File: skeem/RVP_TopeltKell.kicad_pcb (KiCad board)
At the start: 2 copper layers, 106 x 91 mm, 84 parts, among them J1 Barrel_Jack, J10 Conn_01x03_Pin, J11 Conn_01x03_Pin, J12 Conn_01x03_Pin, J13 Conn_01x03_Pin, J14 Conn_01x03_Pin, J15 JST XH 5 pin, J16 JST XH 5 pin, J2 USB_B_Mini, J3 Conn_01x03_Pin, J4 Conn_01x03_Pin, J5 Conn_01x03_Pin, J6 Conn_01x03_Pin, J7 Conn_01x03_Pin, J8 Conn_01x03_Pin, J9 Conn_01x03_Pin, SW1 SW_RESET, U1 AP62200, U10 DRV8428, U11 DRV8428, U2 AP62200, U3 CP2102N-Axx-xQFN24, U4 ESP32-S3-WROOM-1-N4, U5 TLV4961, U6 TLV4961, U7 74LVC2G53, U8 74HCT4851, U9 74HCT4851

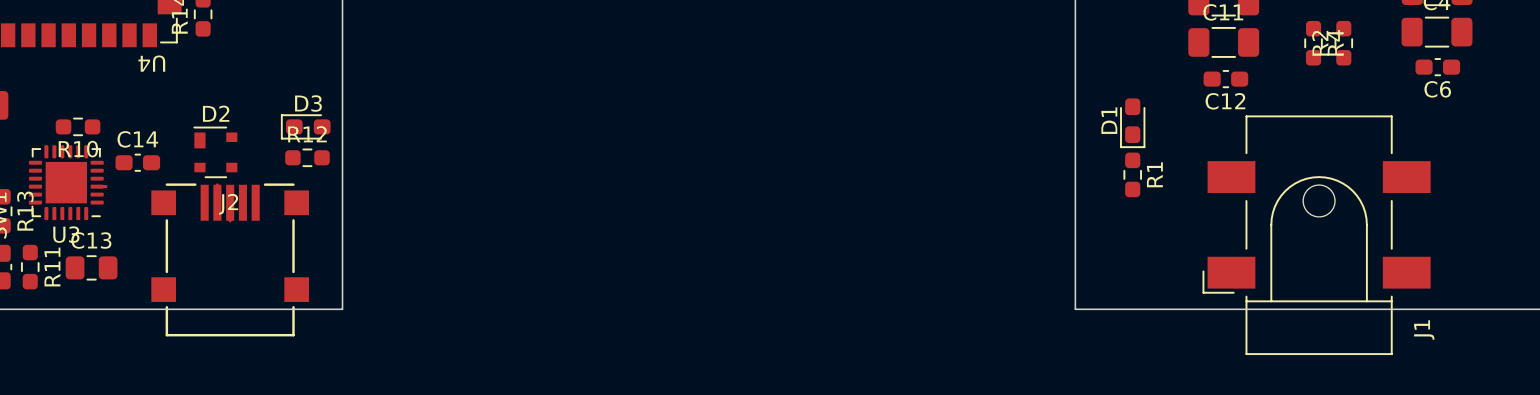
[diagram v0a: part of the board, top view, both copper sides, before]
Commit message: 3d models for pcb
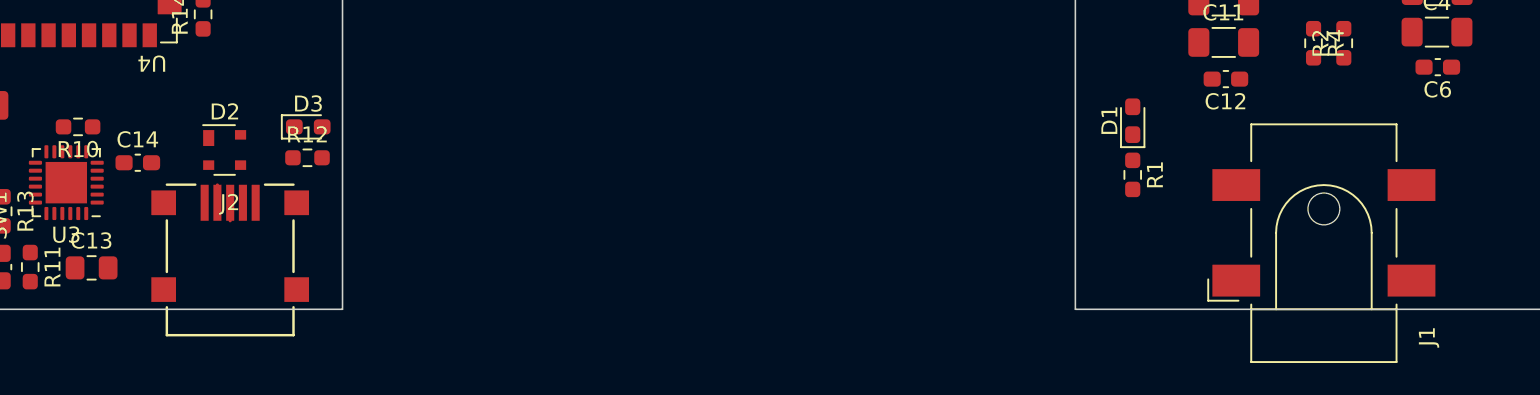
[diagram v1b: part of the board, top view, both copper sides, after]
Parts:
- moved J1 0.58 mm to (200.7, 123.5)
- moved D2 0.57 mm to (131.7, 118.3)
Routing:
- net /D+: track 1.82 -> 1.13 mm
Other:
- board text added: "kas 0.2mm traced? toide?"
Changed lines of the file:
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@@
     (48 "B.Fab" user)
     (49 "F.Fab" user)
-    (50 "User.1" user)
-    (51 "User.2" user)
-    (52 "User.3" user)
-    (53 "User.4" user)
-    (54 "User.5" user)
-    (55 "User.6" user)
-    (56 "User.7" user)
-    (57 "User.8" user)
-    (58 "User.9" user)
   )
   (setup
@@
     (pad "6" smd rect (at -0.95 -1.35) (size 0.7 1) (layers "F.Cu" "F.Paste" "F.Mask")
       (net 7 "Net-(U2-BST)") (pinfunction "BST") (pintype "input") (thermal_bridge_angle 45))
+    (model "${KICAD7_3DMODEL_DIR}/Package_TO_SOT_SMD.3dshapes/SOT-23-6.wrl"
+      (offset (xyz 0 0 0))
+      (scale (xyz 1 1 1))
+      (rotate (xyz 0 0 -90))
+    )
   )
   (footprint "Capacitor_SMD:C_0603_1608Metric_Pad1.08x0.95mm_HandSolder" (layer "F.Cu")
@@
     (pad "3" thru_hole circle (at 0 -5.08) (size 1.44 1.44) (drill 0.8) (layers "*.Cu" "*.Mask")
       (net 2 "GND") (pinfunction "3") (pintype "passive"))
-    (model "${KICAD6_3DMODEL_DIR}/Potentiometer_THT.3dshapes/Potentiometer_Bourns_3386P_Vertical.wrl"
-      (offset (xyz 0 0 0))
+    (model "${KICAD7_3DMODEL_DIR}/Potentiometer_THT.3dshapes/Potentiometer_Bourns_3296Y_Vertical.wrl"
+      (offset (xyz 0 5 0))
       (scale (xyz 1 1 1))
-      (rotate (xyz 0 0 0))
+      (rotate (xyz 0 0 -90))
     )
   )
@@
     (pad "8" smd rect (at -5.774998 5.450078) (size 1.5494 1.5494) (layers "F.Cu" "F.Paste" "F.Mask"))
     (pad "9" smd rect (at 2.574998 5.450078) (size 1.5494 1.5494) (layers "F.Cu" "F.Paste" "F.Mask"))
+    (model "${KICAD7_3DMODEL_DIR}/Connector_USB.3dshapes/USB_Mini-B_Lumberg_2486_01_Horizontal.step"
+      (opacity 0.3500)      (offset (xyz -1.6 -2.5 0))
+      (scale (xyz 1 1 1))
+      (rotate (xyz 0 0 0))
+    )
   )
   (footprint "Capacitor_SMD:C_0805_2012Metric_Pad1.18x1.45mm_HandSolder" (layer "F.Cu")
@@
     (pad "16" smd roundrect (at 2.575 -4.445) (size 1.75 0.6) (layers "F.Cu" "F.Paste" "F.Mask") (roundrect_rratio 0.25)
       (net 5 "+5V") (pinfunction "VCC") (pintype "power_in"))
-    (model "${KICAD6_3DMODEL_DIR}/Package_SO.3dshapes/SO-16_3.9x9.9mm_P1.27mm.wrl"
+    (model "${KICAD7_3DMODEL_DIR}/Package_SO.3dshapes/SOIC-16_3.9x9.9mm_P1.27mm.wrl"
       (offset (xyz 0 0 0))
-      (scale (xyz 1 1 1))
+      (scale (xyz 0.9 1 1))
       (rotate (xyz 0 0 0))
     )
@@
       )
     )
-    (model "${KICAD6_3DMODEL_DIR}/RF_Module.3dshapes/ESP32-S3-WROOM-1.wrl"
+    (model "${KIPRJMOD}/3Dmodels/ESP32-S3-WROOM-1-N16R2.STEP"
       (offset (xyz 0 0 0))
       (scale (xyz 1 1 1))
-      (rotate (xyz 0 0 0))
+      (rotate (xyz -90 0 0))
     )
   )
@@
       (net 5 "+5V") (pinfunction "nSLEEP") (pintype "input"))
     (pad "17" smd rect (at 0 0 270) (size 3 3) (layers "F.Cu" "F.Mask"))
-    (model "${KICAD6_3DMODEL_DIR}/Package_SO.3dshapes/HTSSOP-16-1EP_4.4x5mm_P0.65mm_EP3x3mm.wrl"
+    (model "${KICAD7_3DMODEL_DIR}/Package_SO.3dshapes/MSOP-16-1EP_3x4mm_Pitch0.5mm_EP1.65x2.85mm.wrl"
       (offset (xyz 0 0 0))
-      (scale (xyz 1 1 1))
+      (scale (xyz 1.3 1.3 1))
       (rotate (xyz 0 0 0))
     )
@@
     (pad "6" smd rect (at -0.95 -1.35) (size 0.7 1) (layers "F.Cu" "F.Paste" "F.Mask")
       (net 4 "Net-(U1-BST)") (pinfunction "BST") (pintype "input") (thermal_bridge_angle 45))
+    (model "${KICAD7_3DMODEL_DIR}/Package_TO_SOT_SMD.3dshapes/SOT-23-6.wrl"
+      (offset (xyz 0 0 0))
+      (scale (xyz 1 1 1))
+      (rotate (xyz 0 0 -90))
+    )
   )
   (footprint "Inductor_SMD:L_Wuerth_WE-PD-Typ-7345" (layer "F.Cu")
@@
     (pad "2" smd rect (at 3 0 270) (size 2 1.7) (layers "F.Cu" "F.Paste" "F.Mask")
       (net 5 "+5V") (pinfunction "2") (pintype "passive"))
-    (model "${KICAD6_3DMODEL_DIR}/Inductor_SMD.3dshapes/L_Wuerth_WE-PD-Typ-7345.wrl"
+    (model "${KICAD7_3DMODEL_DIR}/Inductor_SMD.3dshapes/L_Bourns_SRR1260.wrl"
       (offset (xyz 0 0 0))
-      (scale (xyz 1 1 1))
+      (scale (xyz 0.6 0.6 1))
       (rotate (xyz 0 0 0))
     )
@@
       (net 5 "+5V") (pinfunction "nSLEEP") (pintype "input"))
     (pad "17" smd rect (at 0 0 90) (size 3 3) (layers "F.Cu" "F.Mask"))
-    (model "${KICAD6_3DMODEL_DIR}/Package_SO.3dshapes/HTSSOP-16-1EP_4.4x5mm_P0.65mm_EP3x3mm.wrl"
+    (model "${KICAD7_3DMODEL_DIR}/Package_SO.3dshapes/MSOP-16-1EP_3x4mm_Pitch0.5mm_EP1.65x2.85mm.wrl"
       (offset (xyz 0 0 0))
-      (scale (xyz 1 1 1))
+      (scale (xyz 1.3 1.3 1))
       (rotate (xyz 0 0 0))
     )
@@
   )
   (footprint "Connector_BarrelJack:BarrelJack_CLIFF_FC681465S_SMT_Horizontal" (layer "F.Cu")
-    (at 200.4 123 90)
+    (at 200.7 123.5 90)
     (descr "Surface-mount DC Barrel Jack, https://www.cliffuk.co.uk/products/dcconnectors/FC681465S.pdf")
     (tags "Power Jack SMT")
@@
       (net 2 "GND") (pintype "passive"))
     (pad "3" smd rect (at -3 5.5 180) (size 3 2) (layers "F.Cu" "F.Paste" "F.Mask"))
-    (model "${KICAD6_3DMODEL_DIR}/Connector_BarrelJack.3dshapes/BarrelJack_CLIFF_FC681465S_SMT_Horizontal.wrl"
-      (offset (xyz 0 0 0))
+    (model "${KICAD7_3DMODEL_DIR}/Connector_BarrelJack.3dshapes/BarrelJack_Horizontal.wrl"
+      (offset (xyz 6 0 0))
       (scale (xyz 1 1 1))
       (rotate (xyz 0 0 0))
@@
     (pad "16" smd roundrect (at 2.575 -4.445) (size 1.75 0.6) (layers "F.Cu" "F.Paste" "F.Mask") (roundrect_rratio 0.25)
       (net 5 "+5V") (pinfunction "VCC") (pintype "power_in"))
-    (model "${KICAD6_3DMODEL_DIR}/Package_SO.3dshapes/SO-16_3.9x9.9mm_P1.27mm.wrl"
+    (model "${KICAD7_3DMODEL_DIR}/Package_SO.3dshapes/SOIC-16_4.55x10.3mm_P1.27mm.wrl"
       (offset (xyz 0 0 0))
-      (scale (xyz 1 1 1))
+      (scale (xyz 0.8 1 1))
       (rotate (xyz 0 0 0))
     )
@@
   )
   (footprint "Package_TO_SOT_SMD:SOT-143" (layer "F.Cu")
-    (at 131.15 118.45)
+    (at 131.7 118.3)
     (descr "SOT-143 https://www.nxp.com/docs/en/package-information/SOT143B.pdf")
     (tags "SOT-143")
@@
     (pad "2" smd rect (at 3.2 0 270) (size 1.5 2.2) (layers "F.Cu" "F.Paste" "F.Mask")
       (net 8 "+3V3") (pinfunction "2") (pintype "passive"))
-    (model "${KICAD6_3DMODEL_DIR}/Inductor_SMD.3dshapes/L_7.3x7.3_H3.5.wrl"
+    (model "${KICAD7_3DMODEL_DIR}/Inductor_SMD.3dshapes/L_Bourns_SRR1260.wrl"
       (offset (xyz 0 0 0))
-      (scale (xyz 1 1 1))
+      (scale (xyz 0.5 0.5 0.4))
       (rotate (xyz 0 0 0))
     )
@@
     (pad "2" smd rect (at 3.4 2 270) (size 3.2 1) (layers "F.Cu" "F.Paste" "F.Mask")
       (net 9 "/ESP_EN") (pinfunction "2") (pintype "passive"))
-    (model "${KICAD6_3DMODEL_DIR}/Button_Switch_SMD.3dshapes/SW_SPST_EVQQ2.wrl"
+    (model "${KICAD7_3DMODEL_DIR}/Button_Switch_SMD.3dshapes/SW_SPST_PTS645.step"
       (offset (xyz 0 0 0))
-      (scale (xyz 1 1 1))
+      (scale (xyz 0.9 0.9 1))
       (rotate (xyz 0 0 0))
     )
@@
     (effects (font (size 1.5 1.5) (thickness 0.3) bold) (justify left bottom))
   )
+  (gr_text "kas 0.2mm traced?\ntoide?" (at 142.9 113.3) (layer "Cmts.User")
+    (effects (font (size 1 1) (thickness 0.15)) (justify left bottom))
+  )
   (gr_text "kas vaja 100n kondesid\nsisendisse, v2ljundisse?" (at 164.7 108.5) (layer "Cmts.User")
     (effects (font (size 1 1) (thickness 0.15)) (justify left bottom))
@@
     (stroke (width 0.15) (type solid))  )
   (segment (start 131.247699 121.6129) (end 131.247699 120.497699) (width 0.2) (layer "F.Cu") (net 13))
-  (segment (start 132.0477 119.5023) (end 132.15 119.4) (width 0.2) (layer "F.Cu") (net 14))
   (segment (start 132.0477 121.6129) (end 132.0477 122.7432) (width 0.2) (layer "F.Cu") (net 14))
-  (segment (start 124.25 120.6) (end 123.7 120.6) (width 0.2) (layer "F.Cu") (net 14))
 )

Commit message: natuke pcbd
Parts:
- removed H4: MountingHole, MountingHole:MountingHole_3.2mm_M3
- added C28: 100n, Capacitor_SMD:C_0603_1608Metric_Pad1.08x0.95mm_HandSolder, F.Cu at (205.3, 83.4)
- added C29: 100n, Capacitor_SMD:C_0603_1608Metric_Pad1.08x0.95mm_HandSolder, F.Cu at (192.3, 83.3)
- added R8: 470, Resistor_SMD:R_0603_1608Metric_Pad0.98x0.95mm_HandSolder, F.Cu at (118.7, 127.2)
- moved U8 58.3 mm to (181.4, 60.1), turned to 180 degrees
- moved H2 55.8 mm to (211.0, 123.2)
- moved H3 54.7 mm to (189.4, 50.5)
- moved U9 53.7 mm to (176.1, 48.6), turned to 180 degrees
- moved C20 48.6 mm to (179.4, 66.3), turned to 0 degrees
- moved H1 44.0 mm to (118.7, 73.3)
- moved C21 43.5 mm to (174.0, 54.7), turned to 0 degrees
- moved RV1 35.7 mm to (194.3, 57.2), turned to 180 degrees
- moved R20 29.4 mm to (190.0, 66.8), turned to 90 degrees
- moved R11 20.3 mm to (132.7, 110.2), turned to 0 degrees
- moved C22 15.1 mm to (196.3, 90.7), turned to 180 degrees
- moved C13 15.0 mm to (136.3, 118.1), turned to 90 degrees
- moved R12 14.9 mm to (122.6, 123.0), turned to 90 degrees
- moved C25 14.2 mm to (209.8, 92.6), turned to 180 degrees
- moved D3 14.0 mm to (124.4, 123.0), turned to 90 degrees
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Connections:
- C18 pad 1: GND -> Net-(C18-Pad1)
- D2 pad 2: /D- -> /D+
- D2 pad 3: /D+ -> /D-
- D2 pad 4: +5V -> VBUS
- J15 pad 1: /Stepper motors/M1_A1 -> /Stepper motors/M1_B1
- J15 pad 2: /Stepper motors/M1_B1 -> /Stepper motors/M1_B2
- J15 pad 4: /Stepper motors/M1_B2 -> /Stepper motors/M1_A1
- J16 pad 1: /Stepper motors/M2_A1 -> /Stepper motors/M2_B1
- J16 pad 2: /Stepper motors/M2_B1 -> /Stepper motors/M2_B2
- J16 pad 4: /Stepper motors/M2_B2 -> /Stepper motors/M2_A1
- SW1 pad 1: GND -> Net-(C18-Pad1)
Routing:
- net +3V3: track 0.00 -> 218.0 mm, vias 0 -> 4
- net +5V: track 0.00 -> 174.5 mm, vias 0 -> 2
- net +9V: track 0.00 -> 100.6 mm
- net /Stepper motors/VREF: track 0.00 -> 57.7 mm
- net /ESP_EN: track 0.00 -> 51.8 mm, vias 0 -> 4
- net /HALL_HOUR: track 0.00 -> 44.1 mm, vias 0 -> 4
- net /HALL_MINUTE: track 0.00 -> 44.1 mm, vias 0 -> 2
- net /ESP_RXD: track 0.00 -> 37.0 mm, vias 0 -> 2
- net /ESP_TXD: track 0.00 -> 36.0 mm, vias 0 -> 2
- net /EN_DCDC: track 0.00 -> 32.2 mm, vias 0 -> 2
- net VBUS: track 0.00 -> 31.0 mm, vias 0 -> 2
- net /STEP_MINUTE: track 0.00 -> 30.9 mm
- net /STEP_HOUR: track 0.00 -> 29.9 mm
- net /SEL0: track 0.00 -> 29.7 mm
- net /DIR_MINUTE: track 0.00 -> 29.0 mm
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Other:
- board text added: "DEMUXid ikka teisele poole tuua-------"
- board text added: "viib v2limisele hallile lis 5V? lihtsam, ja sobib"
- board text removed: "kas 0.2mm traced? toide?"
- board text removed: "kas vaja 100n kondesid sisendisse, v2ljundisse?"
- board text removed: "kuhu meh augud?"

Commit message: asi
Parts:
- moved U8 36.4 mm to (145.1, 58.1), turned to 0 degrees
- moved C20 32.6 mm to (149.8, 52.5), turned to 90 degrees
- moved J7 32.0 mm to (133.3, 50.1), turned to 90 degrees
- moved U9 31.0 mm to (145.1, 47.3), turned to 0 degrees
- moved C21 30.0 mm to (147.2, 41.2), turned to 180 degrees
- moved J5 28.4 mm to (167.7, 40.2), turned to -90 degrees
- moved J8 27.9 mm to (133.3, 62.0), turned to 90 degrees
- moved J4 22.7 mm to (167.8, 44.4), turned to -90 degrees
- moved J3 17.2 mm to (167.7, 48.4), turned to -90 degrees
- moved J9 16.9 mm to (133.3, 54.0), turned to 90 degrees
- moved J10 16.0 mm to (133.3, 58.1), turned to 90 degrees
- moved J6 11.8 mm to (167.7, 52.5), turned to -90 degrees
- moved J14 8.45 mm to (158.4, 52.4), turned to -90 degrees
- moved J13 8.35 mm to (158.4, 40.7), turned to -90 degrees
- moved J11 2.93 mm to (158.4, 48.5), turned to -90 degrees
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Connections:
- U4 pad 28: /M0_HOUR -> /DIR_HOUR
- U4 pad 29: /M1_HOUR -> /STEP_HOUR
- U4 pad 30: /M0_MINUTE -> /M1_HOUR
- U4 pad 31: /M1_MINUTE -> /M0_HOUR
- U4 pad 32: /DIR_HOUR -> /M0_MINUTE
- U4 pad 33: /DIR_MINUTE -> /M1_MINUTE
- U4 pad 34: /STEP_HOUR -> /STEP_MINUTE
- U4 pad 35: /STEP_MINUTE -> /DIR_MINUTE
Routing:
- net +5V: track 174.5 -> 96.2 mm
- net /SEL0: track 29.7 -> 39.5 mm, vias 0 -> 2
- net /SEL1: track 28.6 -> 37.8 mm, vias 0 -> 2
- net /SEL2: track 27.0 -> 35.9 mm, vias 0 -> 2
- net /Servo motors/SERVO11: track 0.00 -> 7.44 mm
- net /Servo motors/SERVO10: track 0.00 -> 7.04 mm
- net /STEP_HOUR: track 29.9 -> 23.2 mm
- net /Servo motors/SERVO8: track 0.00 -> 6.35 mm
- net /Servo motors/MUX0_OUT1: track 16.6 -> 22.7 mm, vias 0 -> 2
- net /DIR_HOUR: track 27.7 -> 21.7 mm
- net /Servo motors/SERVO9: track 0.00 -> 5.97 mm
- net /Servo motors/MUX0_OUT0: track 25.5 -> 21.5 mm, vias 0 -> 2
- net /M0_HOUR: track 22.1 -> 26.1 mm
- net /M1_MINUTE: track 26.1 -> 29.0 mm
- net /M0_MINUTE: track 25.1 -> 27.7 mm
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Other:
- board text removed: "DEMUXid ikka teisele poole tuua-------"

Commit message: ruuditud v1
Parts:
- moved R10 0.05 mm to (135.2, 114.3)
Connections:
- D2 pad 2: /D+ -> /D-
- D2 pad 3: /D- -> /D+
- R17 pad 2: +3V3 -> +5V
- U10 pad 17: (no net) -> GND
- U11 pad 17: (no net) -> GND
- U4 pad 17: /SEL0 -> /SEL2
- U4 pad 19: /SEL2 -> /SEL0
- U4 pad 32: /M0_MINUTE -> /DIR_MINUTE
- U4 pad 33: /M1_MINUTE -> /STEP_MINUTE
- U4 pad 34: /STEP_MINUTE -> /M1_MINUTE
- U4 pad 35: /DIR_MINUTE -> /M0_MINUTE
- U6 pad 1: +3V3 -> +5V
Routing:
- net GND: track 13.0 -> 193.5 mm, vias 0 -> 32
- net +5V: track 96.2 -> 255.4 mm, vias 2 -> 6
- net /M0_MINUTE: track 27.7 -> 133.3 mm
- net /M1_MINUTE: track 29.0 -> 132.5 mm
- net /STEP_MINUTE: track 29.9 -> 131.1 mm
- net /DIR_MINUTE: track 30.9 -> 129.9 mm
- net /STEP_HOUR: track 23.2 -> 97.5 mm, vias 0 -> 2
- net /M1_HOUR: track 25.1 -> 99.3 mm, vias 0 -> 2
- net /DIR_HOUR: track 21.7 -> 95.6 mm, vias 0 -> 2
- net /M0_HOUR: track 26.1 -> 99.8 mm, vias 0 -> 2
- net /SEL0: track 39.5 -> 83.6 mm, vias 2 -> 4
- net /Servo motors/MUX0_OUT1: track 22.7 -> 66.4 mm
- net /SEL1: track 37.8 -> 78.8 mm
- net /Servo motors/MUX0_OUT0: track 21.5 -> 57.0 mm
- net /SEL2: track 35.9 -> 64.7 mm
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- added copper zone on B.Cu, net GND

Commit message: pisibi valma???
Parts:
- moved R4 64.2 mm to (185.1, 47.8), turned to 90 degrees
- moved R1 63.0 mm to (185.1, 59.7), turned to 90 degrees
- moved R2 60.6 mm to (184.4, 51.2)
- moved C4 59.3 mm to (175.2, 58.4)
- moved C5 59.3 mm to (177.7, 58.4)
- moved C6 59.3 mm to (173.2, 57.6)
- moved L1 59.3 mm to (175.1, 51.3)
- moved C1 59.3 mm to (181.2, 53.2)
- moved C2 59.3 mm to (181.0, 51.2)
- moved C3 59.3 mm to (177.3, 46.0)
- moved R3 59.3 mm to (180.8, 45.0)
- moved R5 59.3 mm to (183.4, 45.9)
- moved U1 59.3 mm to (180.9, 48.1)
- moved D1 56.2 mm to (185.1, 63.1), turned to -90 degrees
- moved U2 39.3 mm to (196.0, 60.9)
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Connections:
- R17 pad 2: +5V -> +3V3
- U4 pad 17: /SEL2 -> unconnected-(U4-IO9-Pad17)
- U4 pad 18: /SEL1 -> unconnected-(U4-IO10-Pad18)
- U4 pad 19: /SEL0 -> unconnected-(U4-IO11-Pad19)
- U4 pad 20: /SEL3 -> /HALL_HOUR
- U4 pad 21: /SERVO_PWM -> /DIR_HOUR
- U4 pad 22: unconnected-(U4-IO14-Pad22) -> /STEP_HOUR
- U4 pad 23: unconnected-(U4-IO21-Pad23) -> /M1_HOUR
- U4 pad 24: unconnected-(U4-IO47-Pad24) -> /M0_HOUR
- U4 pad 25: unconnected-(U4-IO48-Pad25) -> /DIR_MINUTE
- U4 pad 28: /DIR_HOUR -> /STEP_MINUTE
- U4 pad 29: /STEP_HOUR -> /M1_MINUTE
- U4 pad 30: /M1_HOUR -> /M0_MINUTE
- U4 pad 31: /M0_HOUR -> /SEL2
- U4 pad 32: /DIR_MINUTE -> /SEL1
- U4 pad 33: /STEP_MINUTE -> /SEL0
- U4 pad 34: /M1_MINUTE -> /SEL3
- U4 pad 35: /M0_MINUTE -> /SERVO_PWM
- U4 pad 38: unconnected-(U4-IO2-Pad38) -> /HALL_MINUTE
- U4 pad 4: /HALL_HOUR -> unconnected-(U4-IO4-Pad4)
- U4 pad 5: /HALL_MINUTE -> unconnected-(U4-IO5-Pad5)
- U6 pad 1: +5V -> +3V3
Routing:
- net GND: track 193.5 -> 34.5 mm, vias 32 -> 22
- net +9V: track 102.5 -> 141.2 mm
- net /HALL_MINUTE: track 44.0 -> 11.2 mm, vias 2 -> 0
- net /DIR_HOUR: track 95.6 -> 122.5 mm
- net +5V: track 255.4 -> 229.3 mm
- net /STEP_HOUR: track 97.5 -> 122.4 mm
- net /M1_HOUR: track 99.3 -> 122.2 mm
- net /M0_HOUR: track 99.8 -> 121.2 mm
- net /HALL_HOUR: track 44.1 -> 25.0 mm, vias 4 -> 0
- net /SEL2: track 64.7 -> 46.8 mm, vias 2 -> 0
- net /SEL1: track 78.8 -> 61.4 mm, vias 2 -> 0
- net /SEL0: track 83.6 -> 67.7 mm, vias 4 -> 2
- net /Servo motors/MUX0_OUT0: track 57.0 -> 46.0 mm, vias 2 -> 0
- net /Servo motors/MUX0_OUT1: track 66.4 -> 55.6 mm, vias 2 -> 0
- net /SERVO_PWM: track 3.63 -> 10.1 mm
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- added copper zone on F.Cu, net GND
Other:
- board text added: "ESPi GND viad 0.2mm, kas saab puurida?"
- board text added: "kaota LOOP. PAHA"
- board text added: "kas usb norm?"
- board text added: "thermal reliefid eemaldada ground tht delt"
- board text added: "too sissepoole, et gnd oleks plaadi 22rest"
- board text added: "vaata et top pour ei tekita antenne"
- board text added: "viib v2limisele hallile lis 5V? lihtsam, ja sobib EI!!!! esp sureb"
- board text removed: "viib v2limisele hallile lis 5V? lihtsam, ja sobib"
